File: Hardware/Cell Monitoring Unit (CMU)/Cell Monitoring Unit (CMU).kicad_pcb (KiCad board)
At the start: 4 copper layers, 144.7 x 95.9 mm, 167 parts, among them J1 TEST, J10 NTC-5, J11 NTC-6, J12 NTC-7, J13 NTC-8, J2 LOW SIDE, J3 12S, J4 705550056, J5 HIGH SIDE, J6 NTC-1, J7 NTC-2, J8 NTC-3, J9 NTC-4, T1 CEP99-102, T2 CEP99-102, U1 PESD5V0L2BT, U2 PESD5V0L2BT, U3 ZXTN4004KQTC, U4 PBQ79616PAPTQ1

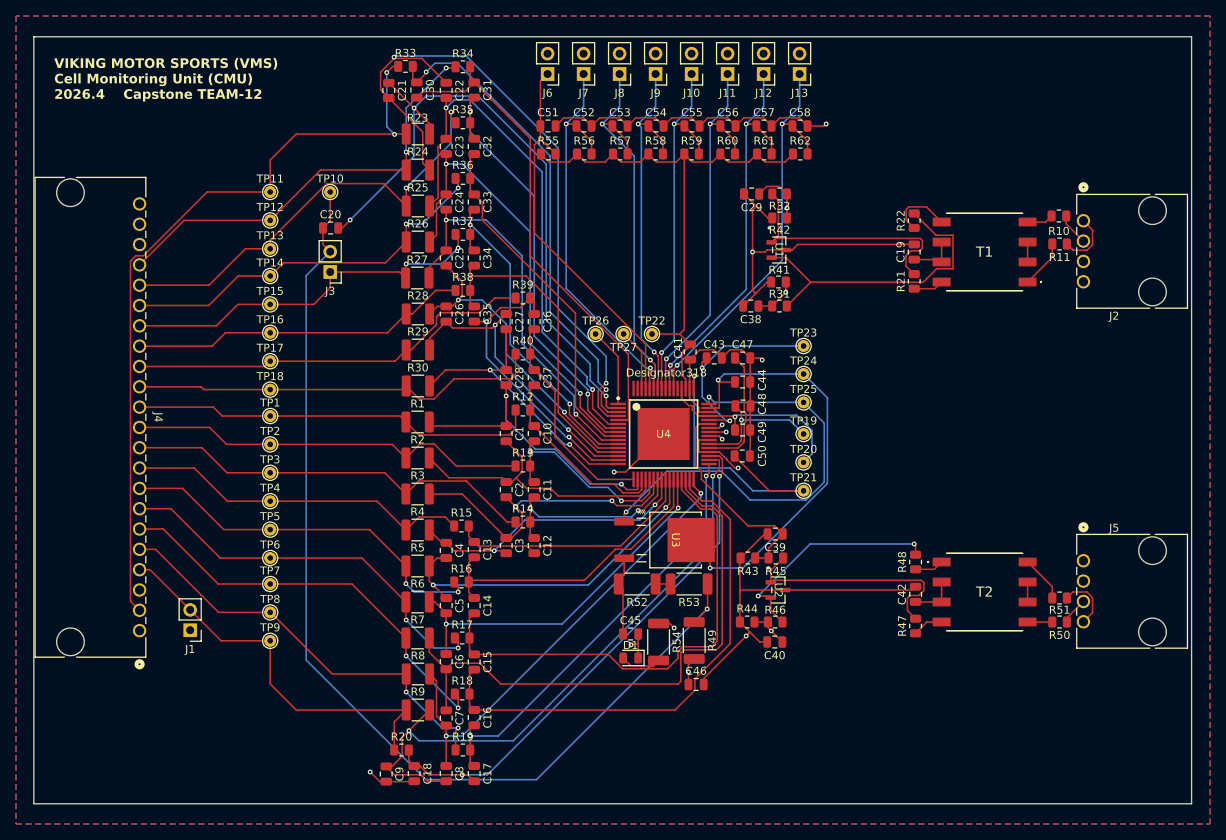
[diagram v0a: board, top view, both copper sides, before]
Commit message: add mounting holes
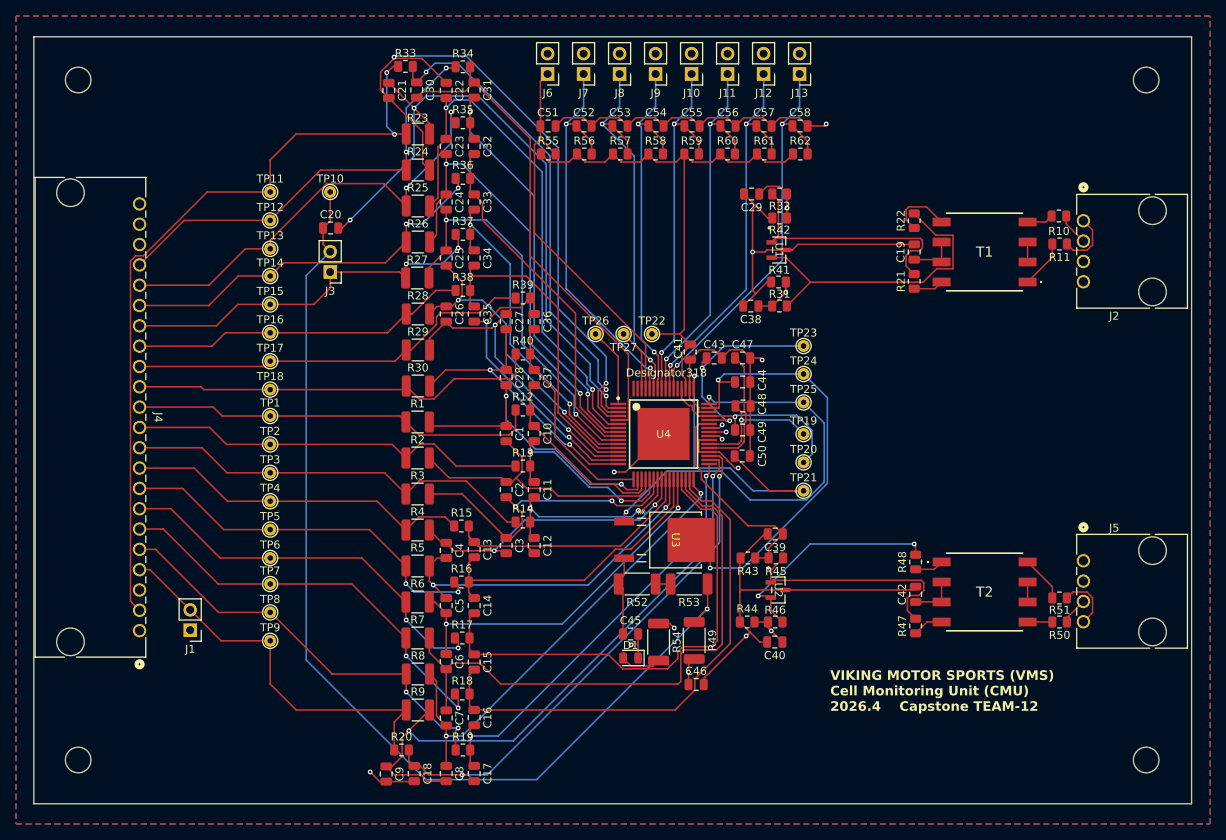
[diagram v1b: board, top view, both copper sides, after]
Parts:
- added REF**: MountingHole_3.2mm_M3, MountingHole:MountingHole_3.2mm_M3, F.Cu at (76.5, 141.5)
- added REF**: MountingHole_3.2mm_M3, MountingHole:MountingHole_3.2mm_M3, F.Cu at (76.5, 56.5)
- added REF**: MountingHole_3.2mm_M3, MountingHole:MountingHole_3.2mm_M3, F.Cu at (210.0, 56.5)
- added REF**: MountingHole_3.2mm_M3, MountingHole:MountingHole_3.2mm_M3, F.Cu at (210.0, 141.5)

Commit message: update layout
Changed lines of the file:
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@@
 		(tags "capacitor")
 		(property "Reference" "C39"
-			(at 0 -1.68 0)
+			(at 0 1.75 0)
 			(layer "F.SilkS")
 			(effects
@@
 	)
 	(segment
-		(start 110.7125 119.5)
-		(end 117.4625 126.25)
-		(width 0.2)
-		(layer "F.Cu")
-		(net "CELL2")
-	)
-	(segment
 		(start 117.4625 128.4625)
 		(end 117.5 128.5)
@@
 	)
 	(segment
-		(start 87.13 112.63)
-		(end 94 119.5)
+		(start 100.5 119.5)
+		(end 103 119.5)
 		(width 0.2)
 		(layer "F.Cu")
@@
 	)
 	(segment
-		(start 100.5 119.5)
-		(end 110.7125 119.5)
+		(start 87.13 112.63)
+		(end 94 119.5)
 		(width 0.2)
 		(layer "F.Cu")
@@
 		(net "CELL2")
 	)
+	(segment
+		(start 103 119.5)
+		(end 109.75 126.25)
+		(width 0.2)
+		(layer "F.Cu")
+		(net "CELL2")
+	)
+	(segment
+		(start 109.75 126.25)
+		(end 117.4625 126.25)
+		(width 0.2)
+		(layer "F.Cu")
+		(net "CELL2")
+	)
 	(via
 		(at 117.5 128.5)
@@
 	)
 	(segment
-		(start 125.325 120.575)
-		(end 125.325 119.25)
+		(start 138.632392 119.025)
+		(end 142.507454 115.149938)
 		(width 0.2)
 		(layer "F.Cu")
@@
 	)
 	(segment
-		(start 125.325 119.025)
-		(end 139.789784 119.025)
+		(start 125.325 120.575)
+		(end 125.325 119.25)
 		(width 0.2)
 		(layer "F.Cu")
@@
 	)
 	(segment
-		(start 125.325 116.825)
-		(end 126 116.15)
+		(start 145.600064 115.149938)
+		(end 150.925483 109.824519)
 		(width 0.2)
 		(layer "F.Cu")
@@
 	)
 	(segment
-		(start 125.325 119.25)
-		(end 125.325 116.825)
+		(start 125.325 119.025)
+		(end 138.632392 119.025)
 		(width 0.2)
 		(layer "F.Cu")
@@
 	)
 	(segment
-		(start 143.664846 115.149938)
-		(end 145.600064 115.149938)
+		(start 125.325 116.825)
+		(end 126 116.15)
 		(width 0.2)
 		(layer "F.Cu")
@@
 	)
 	(segment
-		(start 139.789784 119.025)
-		(end 143.664846 115.149938)
+		(start 125.325 119.25)
+		(end 125.325 116.825)
 		(width 0.2)
 		(layer "F.Cu")
@@
 	)
 	(segment
-		(start 126 121.25)
-		(end 125.325 120.575)
+		(start 142.507454 115.149938)
+		(end 145.600064 115.149938)
 		(width 0.2)
 		(layer "F.Cu")
@@
 	)
 	(segment
-		(start 145.600064 115.149938)
-		(end 150.925483 109.824519)
+		(start 126 121.25)
+		(end 125.325 120.575)
 		(width 0.2)
 		(layer "F.Cu")
@@
 	)
 	(segment
-		(start 122.5 56.85)
-		(end 119.45 53.8)
+		(start 119.5625 66.8875)
+		(end 119.5625 62.9875)
 		(width 0.2)
 		(layer "F.Cu")
@@
 	)
 	(segment
-		(start 119.5625 66.8875)
-		(end 119.5625 62.9875)
+		(start 114.3 55.502756)
+		(end 114.3 57.725)
 		(width 0.2)
 		(layer "F.Cu")
@@
 	)
 	(segment
-		(start 141.5 95.351468)
-		(end 142.451474 94.399994)
+		(start 119.45 53.8)
+		(end 116.002756 53.8)
 		(width 0.2)
 		(layer "F.Cu")
@@
 	)
 	(segment
-		(start 144 98.499999)
-		(end 142.634775 98.499999)
+		(start 141.5 95.351468)
+		(end 142.451474 94.399994)
 		(width 0.2)
 		(layer "F.Cu")
@@
 	)
 	(segment
-		(start 119.5625 62.9875)
-		(end 115.325 58.75)
+		(start 116.002756 53.8)
+		(end 114.3 55.502756)
 		(width 0.2)
 		(layer "F.Cu")
@@
 	)
 	(segment
-		(start 116.002756 53.8)
-		(end 114.3 55.502756)
+		(start 144 98.499999)
+		(end 142.634775 98.499999)
 		(width 0.2)
 		(layer "F.Cu")
@@
 	)
 	(segment
-		(start 114.3 55.502756)
-		(end 114.3 57.725)
+		(start 119.5625 62.9875)
+		(end 115.325 58.75)
 		(width 0.2)
 		(layer "F.Cu")
@@
 	)
 	(segment
-		(start 119.45 53.8)
-		(end 116.002756 53.8)
+		(start 122.5 56.85)
+		(end 119.45 53.8)
 		(width 0.2)
 		(layer "F.Cu")
@@
 	)
 	(segment
-		(start 120.425 67.75)
-		(end 119.5625 66.8875)
+		(start 114.3 57.725)
+		(end 115.325 58.75)
 		(width 0.2)
 		(layer "F.Cu")
@@
 	)
 	(segment
-		(start 141.5 97.365224)
-		(end 141.5 95.351468)
+		(start 120.425 67.75)
+		(end 119.5625 66.8875)
 		(width 0.2)
 		(layer "F.Cu")
@@
 	)
 	(segment
-		(start 114.3 57.725)
-		(end 115.325 58.75)
+		(start 141.5 97.365224)
+		(end 141.5 95.351468)
 		(width 0.2)
 		(layer "F.Cu")

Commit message: update CMU
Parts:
- J2, J5: footprint 705510038:CONN_70551-xxxx_04_MOL -> Footprints:705510038
- J4: footprint Molex 0705550056:CONN_705550000-SD_22_MOL -> Footprints:705550056
- T1, T2: footprint CEP99-102:CEP99102 -> Footprints:CEP99102
- U1, U2: footprint PESD5V0L2BT:SOT23_NEX -> Footprints:SOT23_NEX
- U3: footprint ZXTN4004KTC:DPAK_04KQTC_DIO -> Footprints:DPAK_04KQTC_DIO
- U4: footprint BQ79616PAPRQ1:PAP0064F-IPC_A -> Footprints:PAP0064F-IPC_A
- moved C46 11.8 mm to (159.0, 103.0)
- moved C48 3.80 mm to (159.0, 101.0)
- moved C43 2.80 mm to (159.0, 97.0)
- moved C50 1.58 mm to (159.0, 105.0)
- moved C49 1.39 mm to (158.9, 99.0)
- moved TP22 1.27 mm to (149.5, 88.2)
- moved C42 1.03 mm to (155.0, 91.5), turned to 90 degrees
- moved C41 1.00 mm to (153.0, 91.5), turned to 90 degrees
- renumbered C43 to C42, C44 to C43, C45 to C44, C46 to C45, C47 to C46, C42 to C47, R49 to R47, R47 to R48, R48 to R49, R52 to R50, R53 to R51, R54 to R52, R50 to R53, R51 to R54
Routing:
- net CELL0: track 189.0 -> 12.3 mm, vias 8 -> 67
- net Net-(U4-REFHP): track 15.8 -> 2.91 mm
- net /COMLN_OPT: track 31.6 -> 25.9 mm
- net /COMHP_OPT: track 29.5 -> 24.1 mm
- net Net-(U4-AVDD): track 17.4 -> 12.9 mm, vias 1 -> 0
- net /LDOIN: track 56.4 -> 52.0 mm, vias 2 -> 1
- net Net-(U4-DVDD): track 38.4 -> 35.4 mm
- net /TSREF: track 72.7 -> 69.8 mm
- net Net-(U4-NEG5V): track 26.2 -> 24.3 mm
- net Net-(U4-CVDD): track 64.4 -> 63.1 mm, vias 2 -> 1
- net COMHN: track 35.5 -> 35.0 mm
- net /COMHN_OPT: track 28.9 -> 28.5 mm, vias 2 -> 0
